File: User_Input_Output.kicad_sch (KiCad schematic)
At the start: 39 parts, among them SW10 SW_DIP_x01, SW2 SW_DIP_x01, SW3 SW_DIP_x01, SW4 SW_DIP_x01, SW5 SW_DIP_x01, SW6 SW_DIP_x01, SW7 SW_DIP_x01, SW8 SW_DIP_x01, SW9 SW_DIP_x01

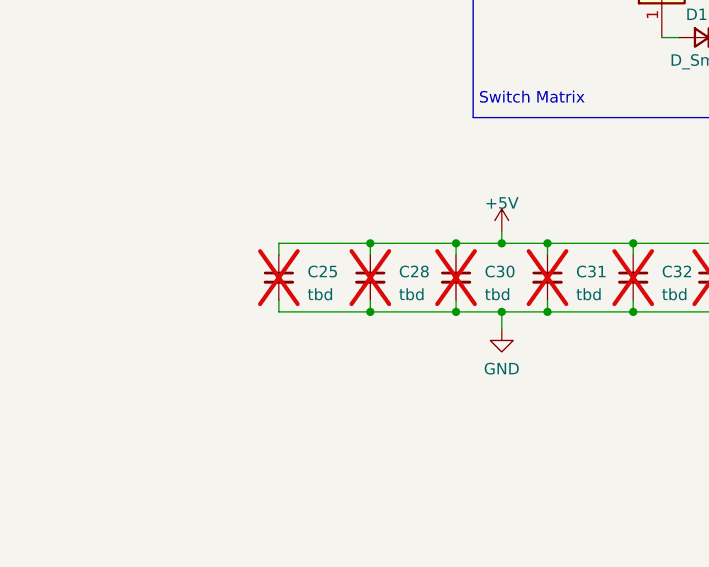
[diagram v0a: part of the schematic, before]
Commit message: Neue Anordnung für bessere Usb Leitungen
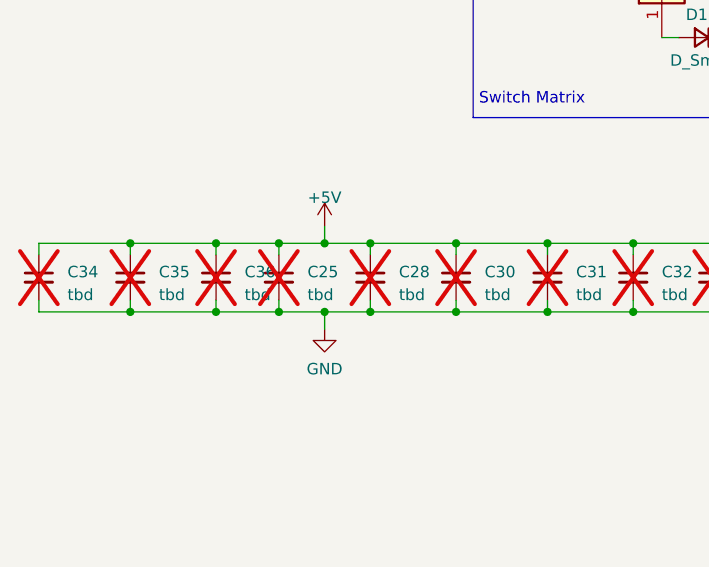
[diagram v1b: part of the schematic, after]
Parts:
- added C34, C35, C36: tbd, Capacitor_SMD:C_0603_1608Metric_Pad1.08x0.95mm_HandSolder, symbol Device:C_Small
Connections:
- net +5V: now also C34.1, C35.1, C36.1
- net GND: now also C34.2, C35.2, C36.2

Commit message: Add files via upload
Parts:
- R15, R16, R2: footprint Resistor_SMD:R_1206_3216Metric_Pad1.30x1.75mm_HandSolder -> Resistor_SMD:R_0805_2012Metric_Pad1.20x1.40mm_HandSolder
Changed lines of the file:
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@@
       (effects (font (size 1.27 1.27)) (justify left))
     )
-    (property "Footprint" "Resistor_SMD:R_1206_3216Metric_Pad1.30x1.75mm_HandSolder" (at 199.517 144.78 90)
+    (property "Footprint" "Resistor_SMD:R_0805_2012Metric_Pad1.20x1.40mm_HandSolder" (at 199.517 144.78 90)
       (effects (font (size 1.27 1.27)) hide)
     )
@@
       (effects (font (size 1.27 1.27)) (justify left))
     )
-    (property "Footprint" "Resistor_SMD:R_1206_3216Metric_Pad1.30x1.75mm_HandSolder" (at 208.407 147.955 90)
+    (property "Footprint" "Resistor_SMD:R_0805_2012Metric_Pad1.20x1.40mm_HandSolder" (at 208.407 147.955 90)
       (effects (font (size 1.27 1.27)) hide)
     )
@@
       (effects (font (size 1.27 1.27)) (justify left))
     )
-    (property "Footprint" "Resistor_SMD:R_1206_3216Metric_Pad1.30x1.75mm_HandSolder" (at 271.907 147.955 90)
-      (effects (font (size 1.27 1.27)) hide)
-    )
+    (property "Footprint" "Resistor_SMD:R_0805_2012Metric_Pad1.20x1.40mm_HandSolder" (at 271.907 147.955 90)
+      (effects (font (size 1.27 1.27)) hide)
+    )

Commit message: Add files via upload
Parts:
- added C9 (x2): 0.1uF, Capacitor_SMD:C_0603_1608Metric_Pad1.08x0.95mm_HandSolder, symbol Device:C
- added R3 (x2): 10k, Resistor_SMD:R_0805_2012Metric_Pad1.20x1.40mm_HandSolder, symbol Device:R
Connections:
- net GND: now also R2.1, C9.2, C9.2; no longer R2.2
- net Rotary_A: now also R3.2; no longer MT1.A
- net Rotary_B: now also R3.2; no longer MT1.B
- net at MT1.2: now also R2.2; no longer R2.1
- new net: C9.1, MT1.A, R3.1
- new net: C9.1, MT1.B, R3.1
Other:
- moved on the sheet: MT1, R2

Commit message: Add STM32 Symbol and changed schematic
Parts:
- removed C9 (x2): 0.1uF, Capacitor_SMD:C_0603_1608Metric_Pad1.08x0.95mm_HandSolder, symbol Device:C
- removed R2: 10k, Resistor_SMD:R_0805_2012Metric_Pad1.20x1.40mm_HandSolder, symbol Device:R
- added C10 (x2): 100nF, Capacitor_SMD:C_0603_1608Metric_Pad1.08x0.95mm_HandSolder, symbol Device:C
- C25, C28, C30, C31, C32, C33, C34, C35, C36: now fitted
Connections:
- net GND: now also C10.1, C10.2
- net at MT1.A, R3.1: now also C10.2
- net at MT1.B, R3.1: now also C10.1
- net BOOT: no longer names the net of MT1.1
- no-connect marks 1 -> 3
